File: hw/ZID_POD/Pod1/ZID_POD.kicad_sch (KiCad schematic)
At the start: 2 parts, among them J1 FFC/FPC-40 Socket

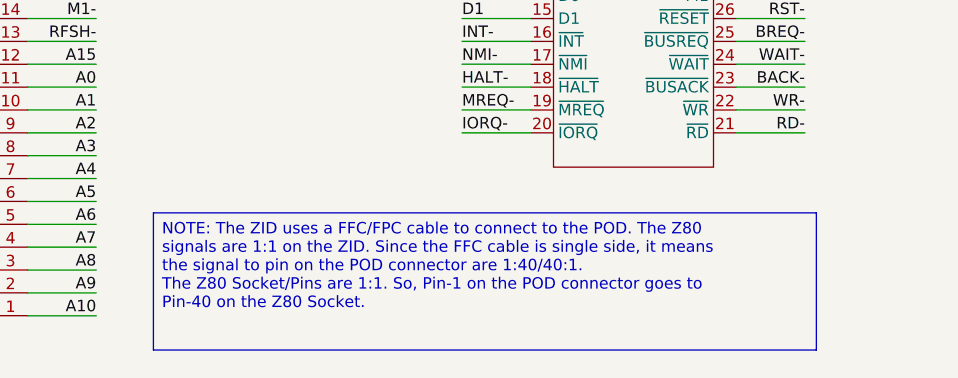
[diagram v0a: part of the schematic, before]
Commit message: PCB: Ready to order - ZID, POD1, POD2, POD3, POD4, ExpBP
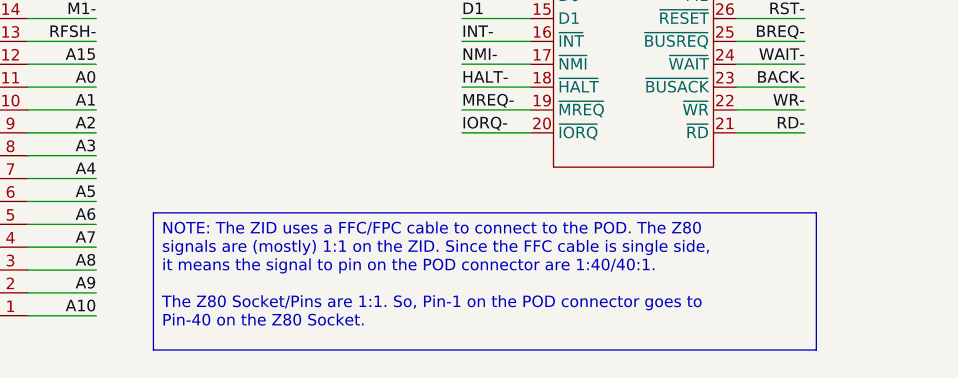
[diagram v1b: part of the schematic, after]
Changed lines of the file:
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@@
 	(title_block
 		(title "ZID POD (1)")
-		(date "2026-04-21")
+		(date "2026-08-16")
 		(rev "PR1.0")
 		(company "SilkyDESIGN")
@@
 		(comment 4 "Layout 1 of 4 to accommodate different")
 	)
-	(text_box "NOTE: The ZID uses a FFC/FPC cable to connect to the POD. The Z80 signals are 1:1 on the ZID. Since the FFC cable is single side, it means the signal to pin on the POD connector are 1:40/40:1.\nThe Z80 Socket/Pins are 1:1. So, Pin-1 on the POD connector goes to Pin-40 on the Z80 Socket."
+	(text_box "NOTE: The ZID uses a FFC/FPC cable to connect to the POD. The Z80 signals are (mostly) 1:1 on the ZID. Since the FFC cable is single side, it means the signal to pin on the POD connector are 1:40/40:1.\n\nThe Z80 Socket/Pins are 1:1. So, Pin-1 on the POD connector goes to Pin-40 on the Z80 Socket."
 		(exclude_from_sim no)
 		(at 124.46 139.7 0)
